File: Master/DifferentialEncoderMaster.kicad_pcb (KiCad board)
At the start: 4 copper layers, 131 x 46.5 mm, 53 parts, among them J1 RJ45_Shielded_x2, J10 Encoder_0, J11 Encoder_1, J12 CAN_Header, J13 ISO_GPIO, J2 Conn_01x06, J3 Conn_01x20, J4 Conn_01x12, J5 RJ45_Shielded_x2, J8 Jumper, J9 Jumper, U1 SN75C1167, U2 SN75C1167, U3 ST26C32ABTR, U4 ST26C32ABTR, U6 ISO7761DBQ

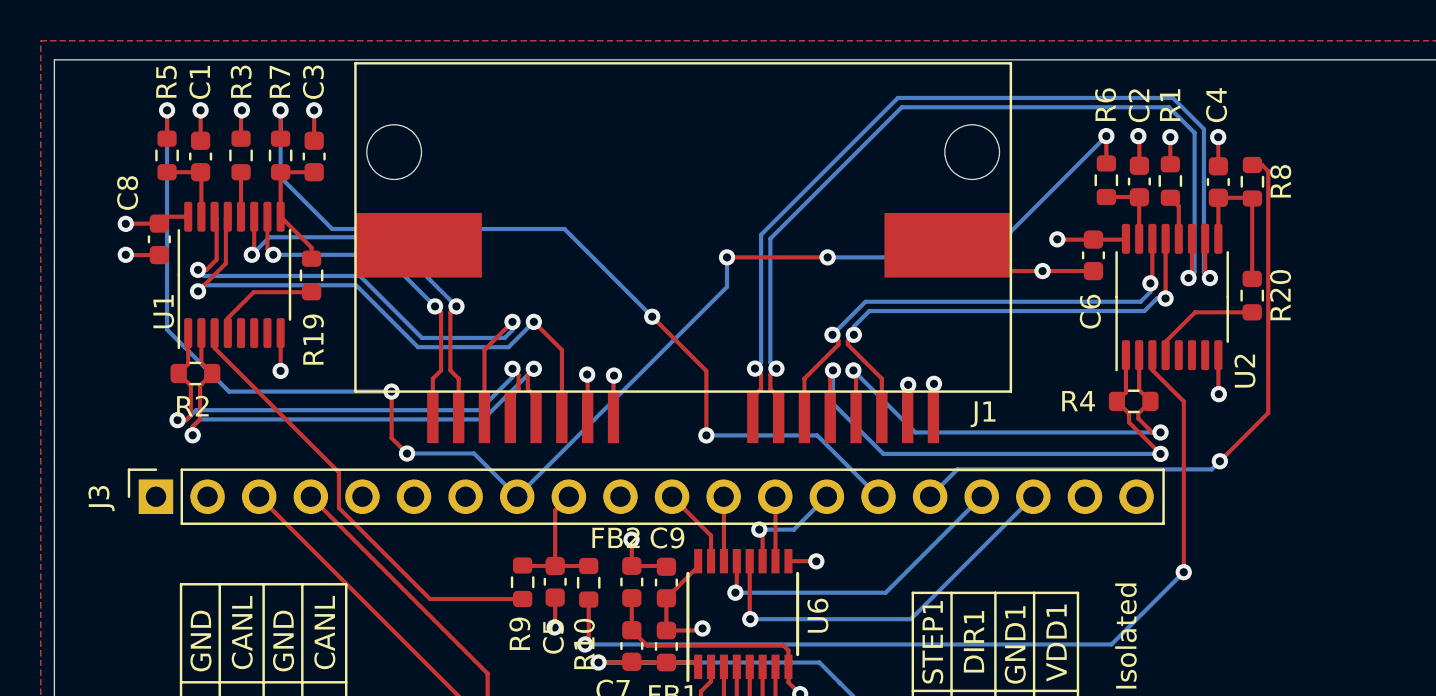
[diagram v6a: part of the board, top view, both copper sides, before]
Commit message: Odrive side TSSOP->SSOP
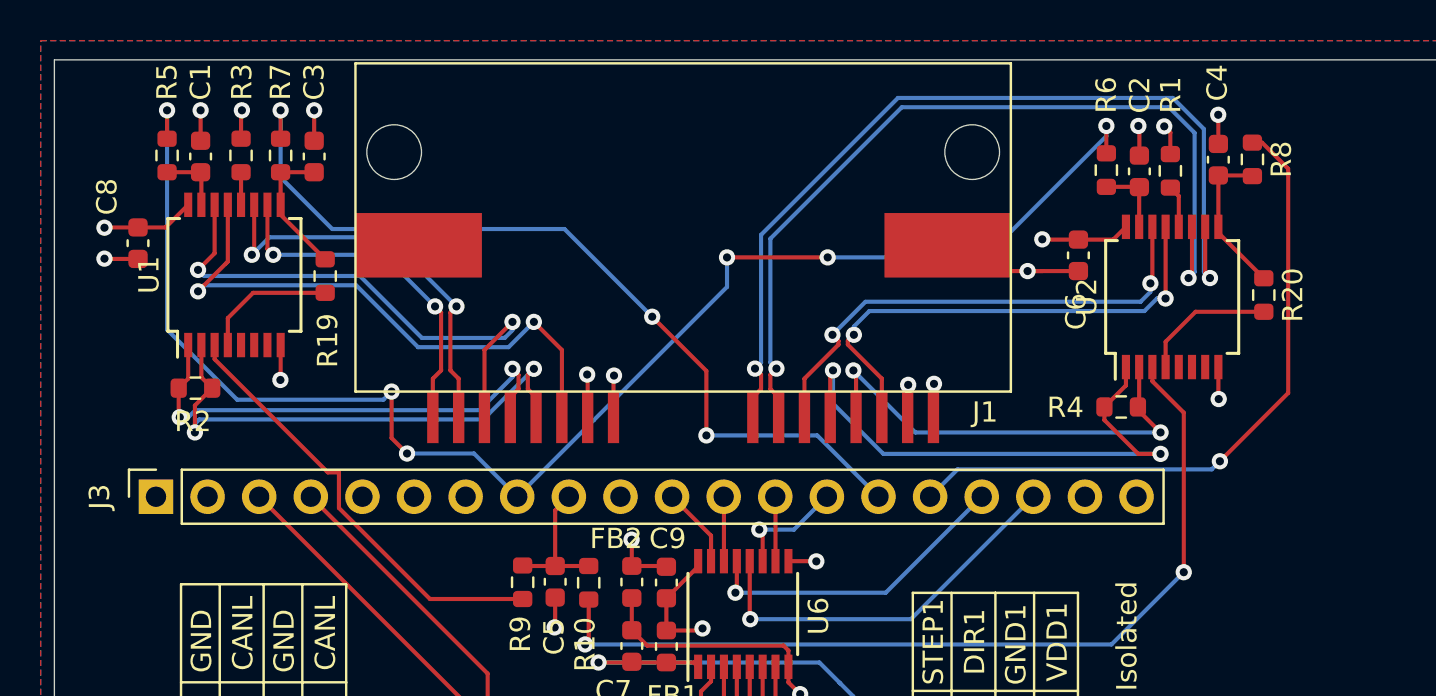
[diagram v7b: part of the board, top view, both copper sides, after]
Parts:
- U1, U2: footprint Package_SO:TSSOP-16_4.4x5mm_P0.65mm -> Package_SO:SSOP-16_5.3x6.2mm_P0.65mm
- moved R8 1.10 mm to (123.1, 61.7)
- moved C4 1.10 mm to (121.5, 61.7)
- moved C8 1.07 mm to (68.3, 65.8)
- moved C6 0.74 mm to (114.6, 66.4)
- moved R2 0.72 mm to (71.1, 73.0)
- moved R4 0.68 mm to (116.7, 73.9)
- moved R19 0.67 mm to (77.5, 67.5)
- moved R20 0.57 mm to (123.7, 68.4)
- moved C2 0.50 mm to (117.6, 62.3)
- moved R1 0.50 mm to (119.1, 62.3)
- moved R6 0.50 mm to (116.0, 62.3)
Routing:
- net +5V: track 36.7 -> 39.5 mm
- net /GPIO6: track 31.2 -> 33.1 mm
- net /MISO_1-: track 25.7 -> 24.1 mm
- net /MISO_2+: track 23.7 -> 22.5 mm
- net /MISO_1+: track 26.7 -> 25.8 mm
- net /SCK: track 72.7 -> 73.5 mm
- net Net-(R19-Pad2): track 5.39 -> 6.04 mm
- net /MISO_2: track 44.5 -> 44.0 mm
- net /CSn_2-: track 42.6 -> 43.1 mm
- net /CSn_2+: track 44.1 -> 44.7 mm
- net /CLK_2-: track 24.1 -> 24.7 mm
- net /CLK_2+: track 24.1 -> 24.6 mm
- net Net-(R3-Pad2): track 2.19 -> 1.61 mm
- net /CLK_1-: track 28.0 -> 28.6 mm
- net /CLK_1: track 3.86 -> 3.27 mm
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
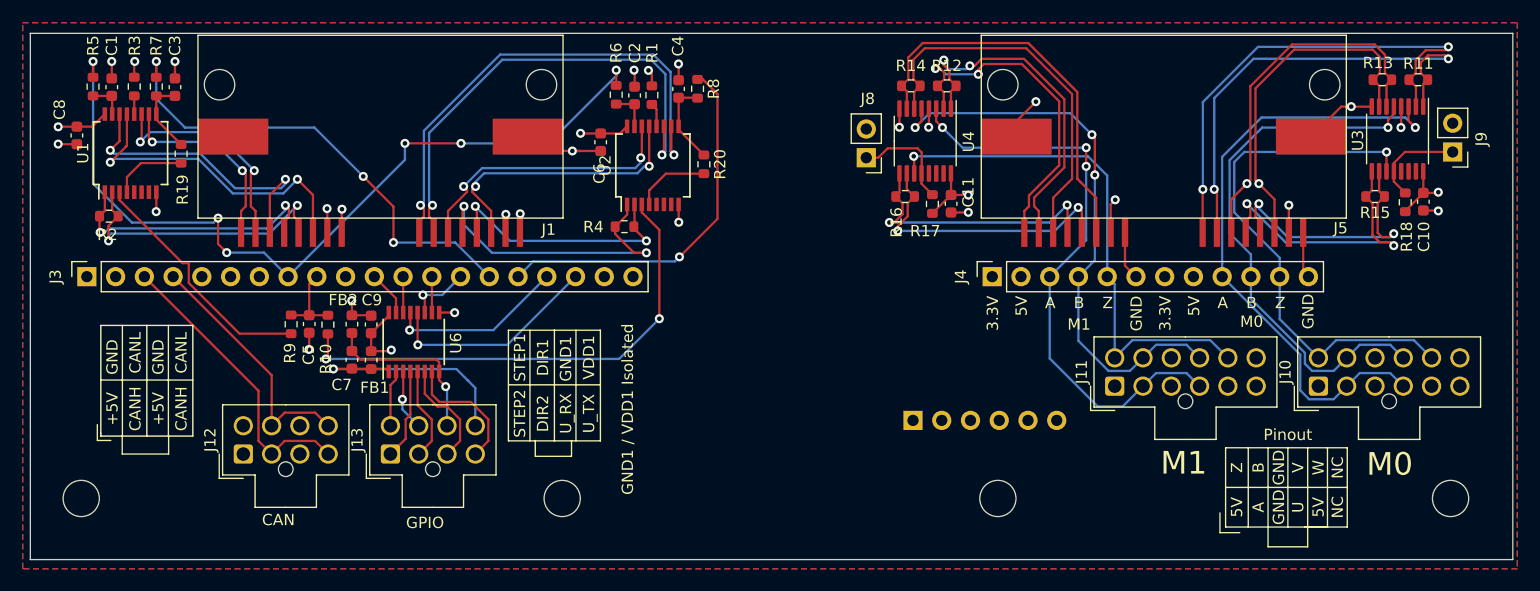
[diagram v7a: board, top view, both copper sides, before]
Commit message: Remove differential encoder half
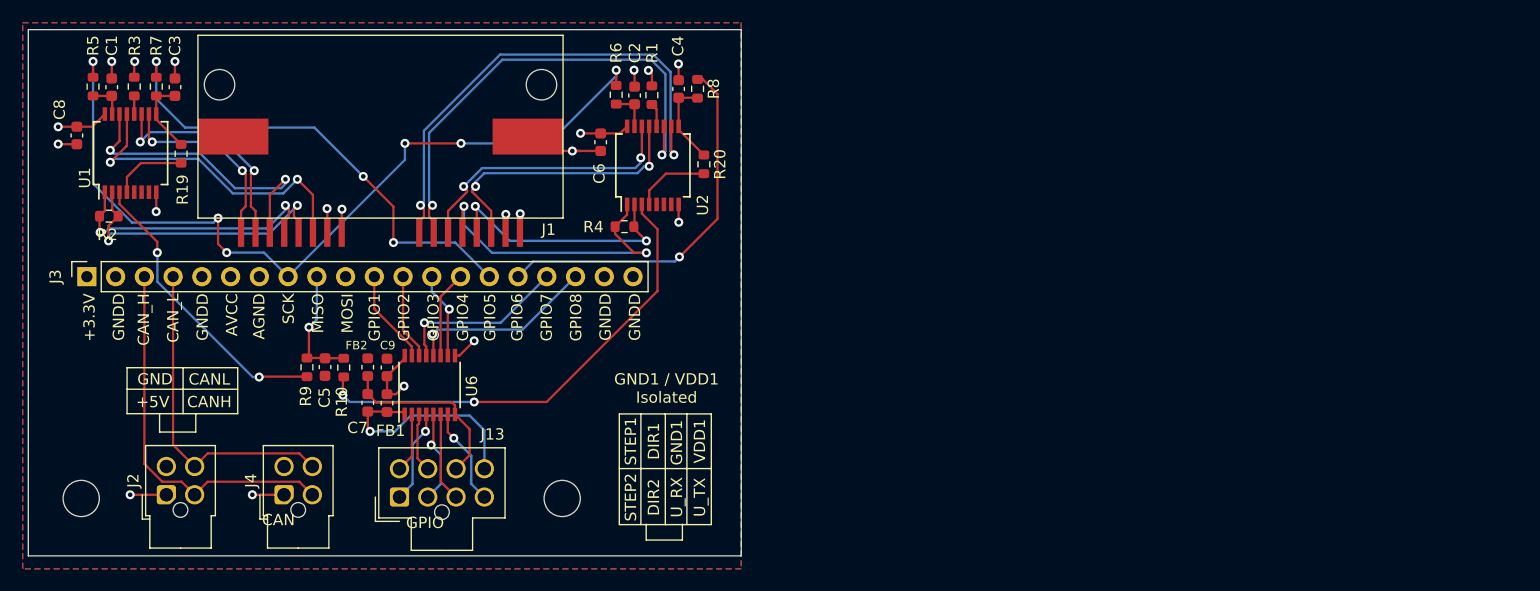
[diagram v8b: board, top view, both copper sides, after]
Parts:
- removed C10, C11: 100nF, Capacitor_SMD:C_0603_1608Metric
- removed H3, H4: MountingHole, MountingHole:MountingHole_3.2mm_M3
- removed J10: Encoder_0, Connector_Molex:Molex_Nano-Fit_105310-xx12_2x06_P2.50mm_Vertical
- removed J11: Encoder_1, Connector_Molex:Molex_Nano-Fit_105310-xx12_2x06_P2.50mm_Vertical
- removed J12: CAN_Header, Connector_Molex:Molex_Nano-Fit_105310-xx08_2x04_P2.50mm_Vertical
- removed J5: RJ45_Shielded_x2, Wetmelon:RJ45_RJSSE5380-02
- removed J8, J9: Jumper, Connector_PinHeader_2.54mm:PinHeader_1x02_P2.54mm_Vertical
- removed R11, R12, R13, R14, R15, R16: 100, Resistor_SMD:R_0603_1608Metric
- removed R17, R18: 3.3k, Resistor_SMD:R_0603_1608Metric
- removed U3, U4: ST26C32ABTR, Package_SO:TSSOP-16_4.4x5mm_P0.65mm
- J2: value Conn_01x06 -> CAN; footprint Connector_PinSocket_2.54mm:PinSocket_1x06_P2.54mm_Vertical -> Connector_Molex:Molex_Nano-Fit_105310-xx04_2x02_P2.50mm_Vertical; moved to F.Cu
- J4: value Conn_01x12 -> CAN; footprint Connector_PinSocket_2.54mm:PinSocket_1x12_P2.54mm_Vertical -> Connector_Molex:Molex_Nano-Fit_105310-xx04_2x02_P2.50mm_Vertical
- moved J2 66.3 mm to (76.2, 97.6), turned to 90 degrees
- moved J4 65.5 mm to (86.6, 97.6)
- moved C7 4.05 mm to (94.0, 89.5)
- moved C9 4.05 mm to (95.7, 86.3)
- moved FB1 4.05 mm to (95.7, 89.5)
- moved FB2 4.05 mm to (94.0, 86.3)
- moved U6 4.05 mm to (99.5, 87.9)
- moved C5 4.05 mm to (90.2, 86.3)
- moved R10 4.05 mm to (91.9, 86.4)
- moved R9 4.05 mm to (88.6, 86.3)
- moved J13 3.88 mm to (96.8, 97.8)
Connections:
- J2 pad 2: (no net) -> /CAN_H
- J2 pad 3: (no net) -> GNDD
- J2 pad 4: GNDD -> /CAN_L
- J4 pad 1: (no net) -> +5V
- J4 pad 2: +5V -> /CAN_H
- J4 pad 3: /M1_A -> GNDD
- J4 pad 4: /M1_B -> /CAN_L
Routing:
- net /M0_A: track 55.3 -> 0.00 mm, vias 1 -> 0
- net /M1_A: track 52.0 -> 0.00 mm, vias 3 -> 0
- net /M1_B: track 51.0 -> 0.00 mm, vias 3 -> 0
- net /M0_B: track 48.4 -> 0.00 mm, vias 1 -> 0
- net /M0_Z: track 47.2 -> 0.00 mm, vias 1 -> 0
- net /M1_Z: track 47.0 -> 0.00 mm, vias 1 -> 0
- net /ENC0_A+: track 43.2 -> 0.00 mm, vias 2 -> 0
- net /ENC0_A-: track 41.2 -> 0.00 mm, vias 2 -> 0
- net /ENC1_B-: track 35.3 -> 0.00 mm
- net /ENC1_B+: track 33.8 -> 0.00 mm
- net /ENC0_B+: track 32.4 -> 0.00 mm, vias 1 -> 0
- net /ENC1_A-: track 31.1 -> 0.00 mm, vias 2 -> 0
- net /ENC0_B-: track 31.0 -> 0.00 mm, vias 1 -> 0
- net /ENC1_A+: track 30.6 -> 0.00 mm, vias 2 -> 0
- net GNDD: track 56.2 -> 25.8 mm, vias 20 -> 11
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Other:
- board size 131 x 46.5 mm -> 63 x 46.5 mm
- board text added: "+3.3V"
- board text added: "AGND"
- board text added: "AVCC"
- board text added: "CAN_H"
- board text added: "CAN_L"
- board text added: "GNDD"
- board text added: "GPIO1"
- board text added: "GPIO2"
- board text added: "GPIO3"
- board text added: "GPIO4"
- board text added: "GPIO5"
- board text added: "GPIO6"
- board text added: "GPIO7"
- board text added: "GPIO8"
- board text added: "MISO"
- board text added: "MOSI"
- board text added: "SCK"
- board text removed: "3.3V"
- board text removed: "5V"
- board text removed: "A"
- board text removed: "B"
- board text removed: "M0"
- board text removed: "M1"
- board text removed: "NC"
- board text removed: "Pinout"
- board text removed: "U"
- board text removed: "V"
- board text removed: "W"
- board text removed: "Z"
